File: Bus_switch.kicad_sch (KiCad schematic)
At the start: 8 parts, among them J3 Conn_01x04_Pin, U1 SN74CB3Q3384APW

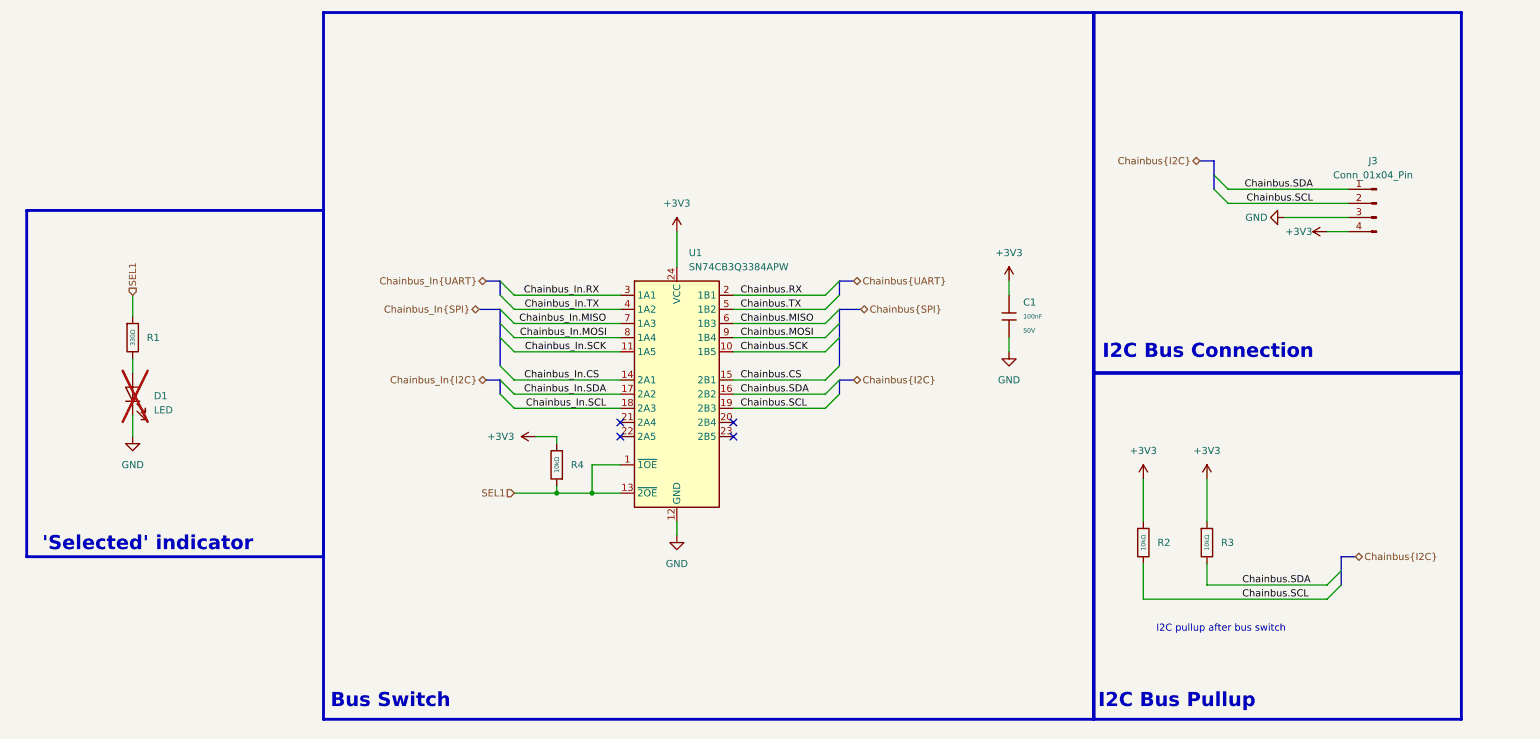
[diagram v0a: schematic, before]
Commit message: updated routing, removed megamind
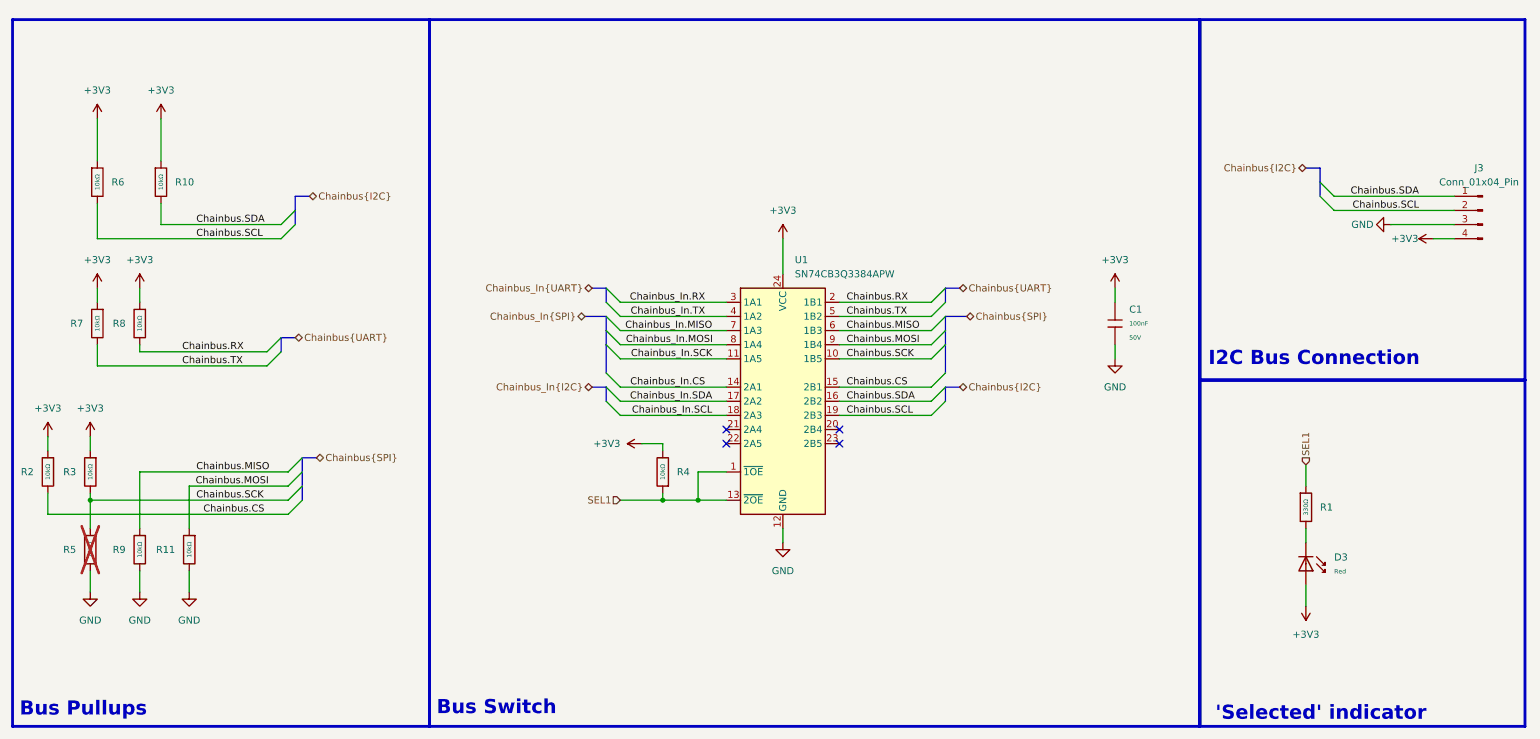
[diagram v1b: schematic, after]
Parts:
- removed D1: LED, LED_SMD:LED_0603_1608Metric, symbol Device:LED
- added D3: Red, PCM_JLCPCB:D_0603, symbol PCM_JLCPCB-Diodes:LED,0603,Red
- added R10, R11, R5, R6, R7, R8, R9: 10kΩ, PCM_JLCPCB:R_0402, symbol PCM_JLCPCB-Resistors:0402,10kΩ
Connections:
- net +3V3: now also D3.2, R10.1, R6.1, R7.1, R8.1
- net Chainbus.CS: now also R2.2
- net Chainbus.MISO: now also R9.1
- net Chainbus.MOSI: now also R11.1
- net Chainbus.RX: now also R8.2
- net Chainbus.SCK: now also R3.2, R5.1
- net Chainbus.SCL: now also R6.2; no longer R2.2
- net Chainbus.SDA: now also R10.2; no longer R3.2
- net Chainbus.TX: now also R7.2
- net GND: now also R11.2, R5.2, R9.2
- net at R1.2: now also D3.1
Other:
- note added: "Bus Pullups"
- note removed: "I2C Bus Pullup"
- note removed: "I2C pullup after bus switch"
- company: (none) -> Moducard System
